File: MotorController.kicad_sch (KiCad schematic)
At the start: 103 parts, among them IC1 ft234xd, IC2 A3921KLPTR-T, IC3 A3921KLPTR-T, J1 Conn_01x04, J10 Conn_01x02, J2 USB_B_Micro, J3 Conn_01x02, J4 8P8C, J5 Conn_01x02, J6 Conn_01x04, J7 Conn_01x04, J8 Conn_01x02, J9 Conn_01x06, Q1 GSFQ6806, Q2 GSFQ6806, Q3 GSFQ6806, Q4 GSFQ6806, Q5 Q_PMOS_GDSD, SW1 SW_Push, SW2 SW_DPDT_x2, U1 LXES11D, U2 STM32F303K8Tx, U3 TJA11441AT, U4 TPSM13604HNDWR, U5 LMZ12002EXT, Y1 32M

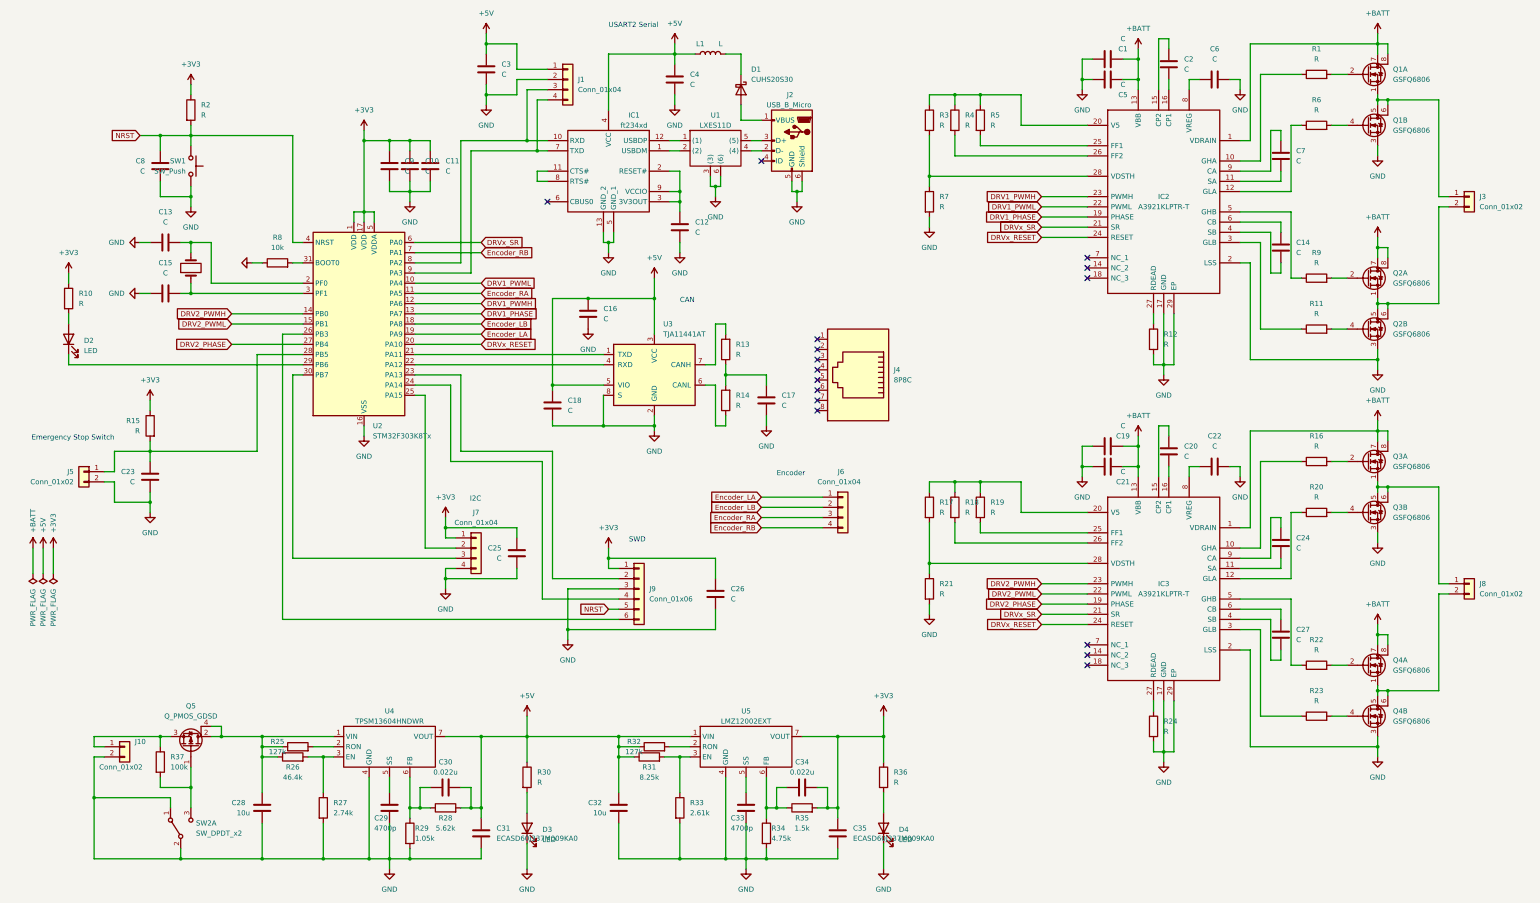
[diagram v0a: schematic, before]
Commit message: CAN 通信周りの端子の変更と電源スイッチの回路図を変更
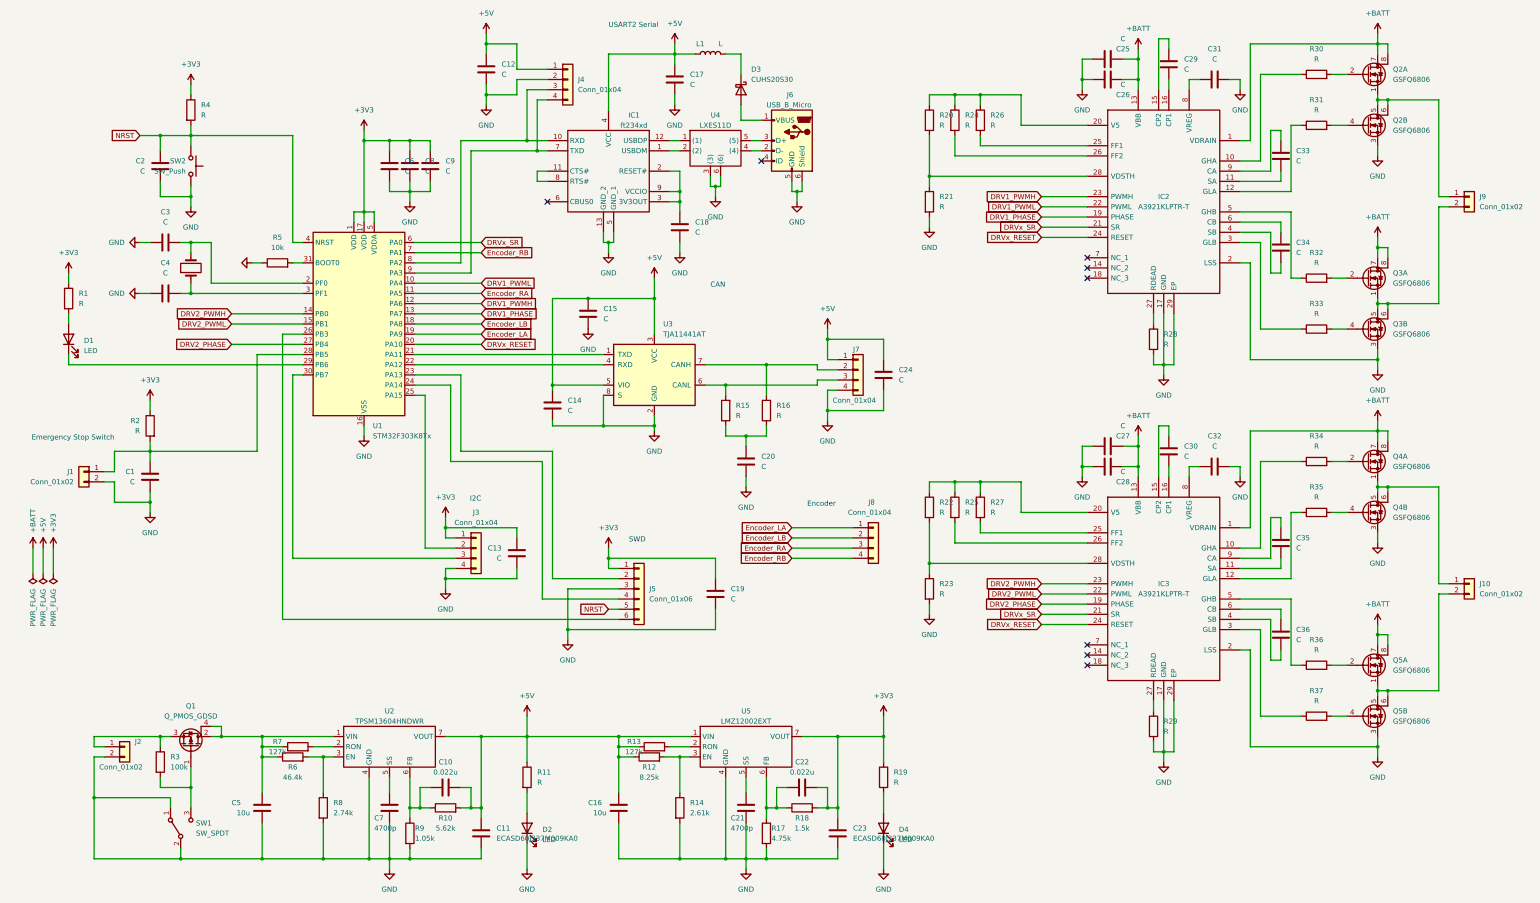
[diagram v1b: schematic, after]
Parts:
- removed C17: C, symbol Device:C
- removed J4: 8P8C, symbol Connector:8P8C
- removed SW2: SW_DPDT_x2, symbol Switch:SW_DPDT_x2
- added C20, C24: C, symbol Device:C
- added J7: Conn_01x04, symbol Connector_Generic:Conn_01x04
- added SW1: SW_SPDT, symbol Switch:SW_SPDT
- renumbered C23 to C1, C30 to C10, C31 to C11, C3 to C12, C25 to C13, C18 to C14, C16 to C15, C32 to C16, C4 to C17, C12 to C18, C26 to C19, C8 to C2, C33 to C21, C34 to C22, C35 to C23, C1 to C25, C5 to C26, C19 to C27, C21 to C28, C2 to C29, C13 to C3, C20 to C30, C6 to C31, C22 to C32, C7 to C33, C14 to C34, C24 to C35, C27 to C36, C15 to C4, C28 to C5, C9 to C6, C29 to C7, C10 to C8, C11 to C9, D2 to D1, D3 to D2, D1 to D3, J5 to J1, J8 to J10, J10 to J2, J7 to J3, J1 to J4, J9 to J5, J2 to J6, J6 to J8, J3 to J9, Q5 to Q1, Q1 to Q2, Q2 to Q3, Q3 to Q4, Q4 to Q5, R10 to R1, R28 to R10, R30 to R11, R31 to R12, R32 to R13, R33 to R14, R14 to R15, R13 to R16, R34 to R17, R35 to R18, R36 to R19, R15 to R2, R3 to R20, R7 to R21, R17 to R22, R21 to R23, R4 to R24, R18 to R25, R5 to R26, R19 to R27, R12 to R28, R24 to R29, R37 to R3, R1 to R30, R6 to R31, R9 to R32, R11 to R33, R16 to R34, R20 to R35, R22 to R36, R23 to R37, R2 to R4, R8 to R5, R26 to R6, R25 to R7, R27 to R8, R29 to R9, SW1 to SW2, U2 to U1, U4 to U2, U1 to U4
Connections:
- net +5V: now also C24.1, J7.1 (Pin_1)
- net GND: now also C20.2, C24.2, J7.4 (Pin_4), SW1.1 (A), SW1.2 (B)
- net at Q1.1 (G), R3.2: now also SW1.3 (C)
- net at R15.2: now also U3.6 (CANL), J7.3 (Pin_3); no longer R16.1
- net at R15.1: now also R16.1, C20.1; no longer U3.6 (CANL)
- net at R16.2, U3.7 (CANH): now also J7.2 (Pin_2)
- no-connect marks 16 -> 8
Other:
- moved on the sheet: J8, R15, R16

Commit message: 先輩に見せるためにいったんコミット。コネクタの回路図とか変えた
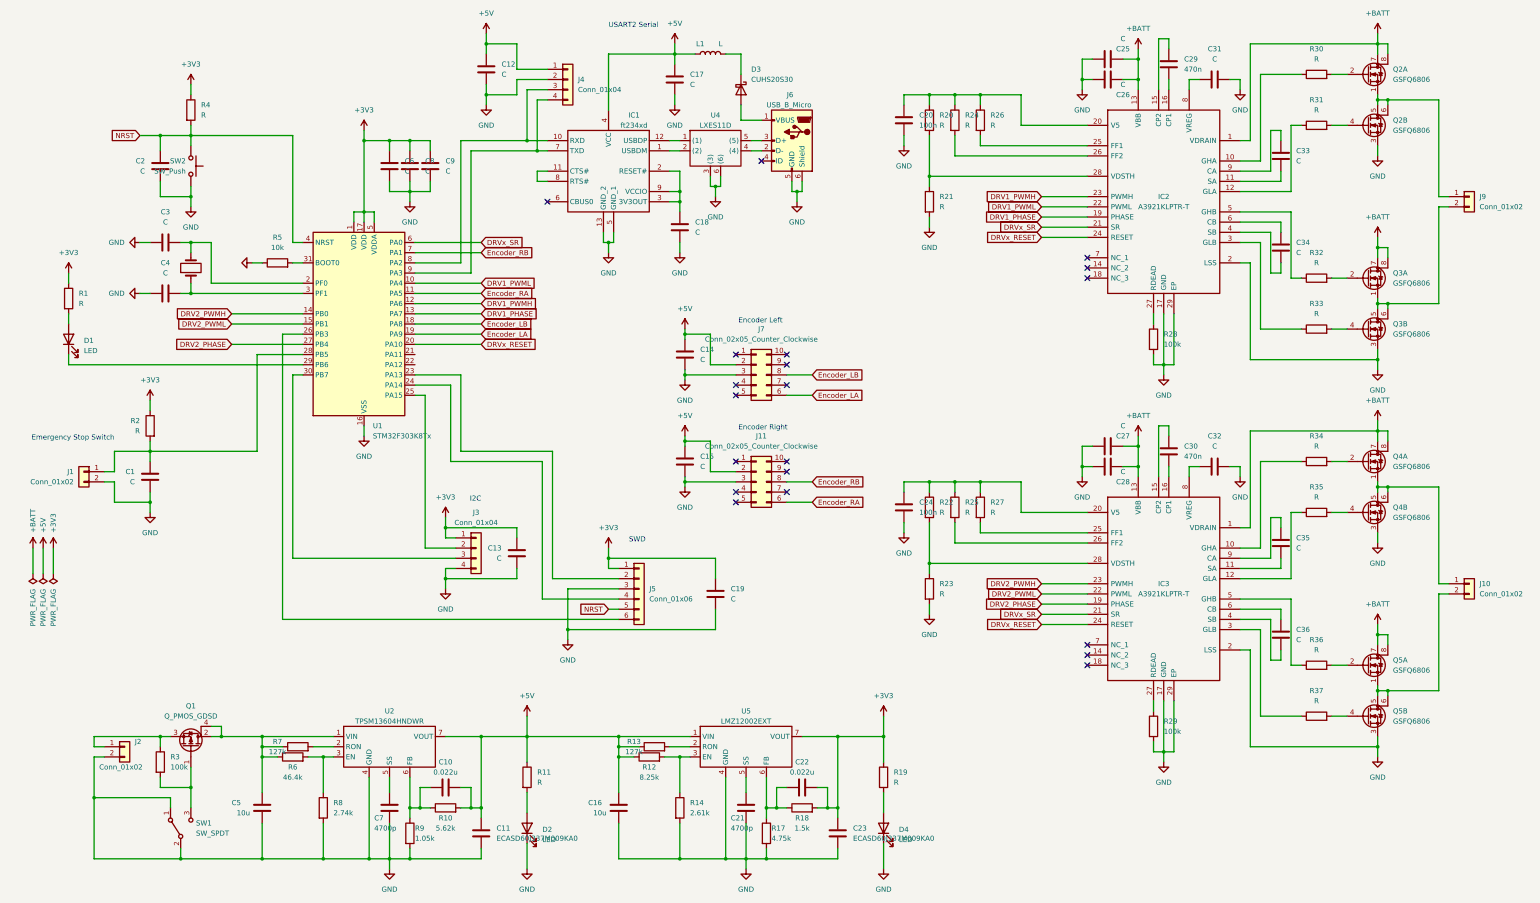
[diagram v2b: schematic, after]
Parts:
- removed J7, J8: Conn_01x04, symbol Connector_Generic:Conn_01x04
- removed R15, R16: R, symbol Device:R
- removed U3: TJA11441AT, Package_SO:SOIC-8_3.9x4.9mm_P1.27mm, symbol Interface_CAN_LIN:TJA1051T-3
- added J11, J7: Conn_02x05_Counter_Clockwise, symbol Connector_Generic:Conn_02x05_Counter_Clockwise
- C20, C24: value C -> 100n
- C29, C30: value C -> 470n
- R28, R29: value R -> 100k
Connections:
- net +5V: now also J11.2 (Pin_2), J7.2 (Pin_2); no longer C24.1
- net Encoder_LA: now also J7.6 (Pin_6)
- net Encoder_LB: now also J7.8 (Pin_8)
- net Encoder_RA: now also J11.6 (Pin_6)
- net Encoder_RB: now also J11.8 (Pin_8)
- net GND: now also J11.3 (Pin_3), J7.3 (Pin_3)
- net at IC3.20 (V5), R22.1, R25.1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: now also C24.1
- net at IC2.20 (V5), R20.1, R24.1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: now also C20.1
- no-connect marks 8 -> 20
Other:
- note added: "Encoder Left"
- note added: "Encoder Right"
- note removed: "CAN"
- note removed: "Encoder"

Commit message: A3921 の回路を訂正・USB 5V から DCDC 5V に入り込まないようにした・IC1 にパスコン追加
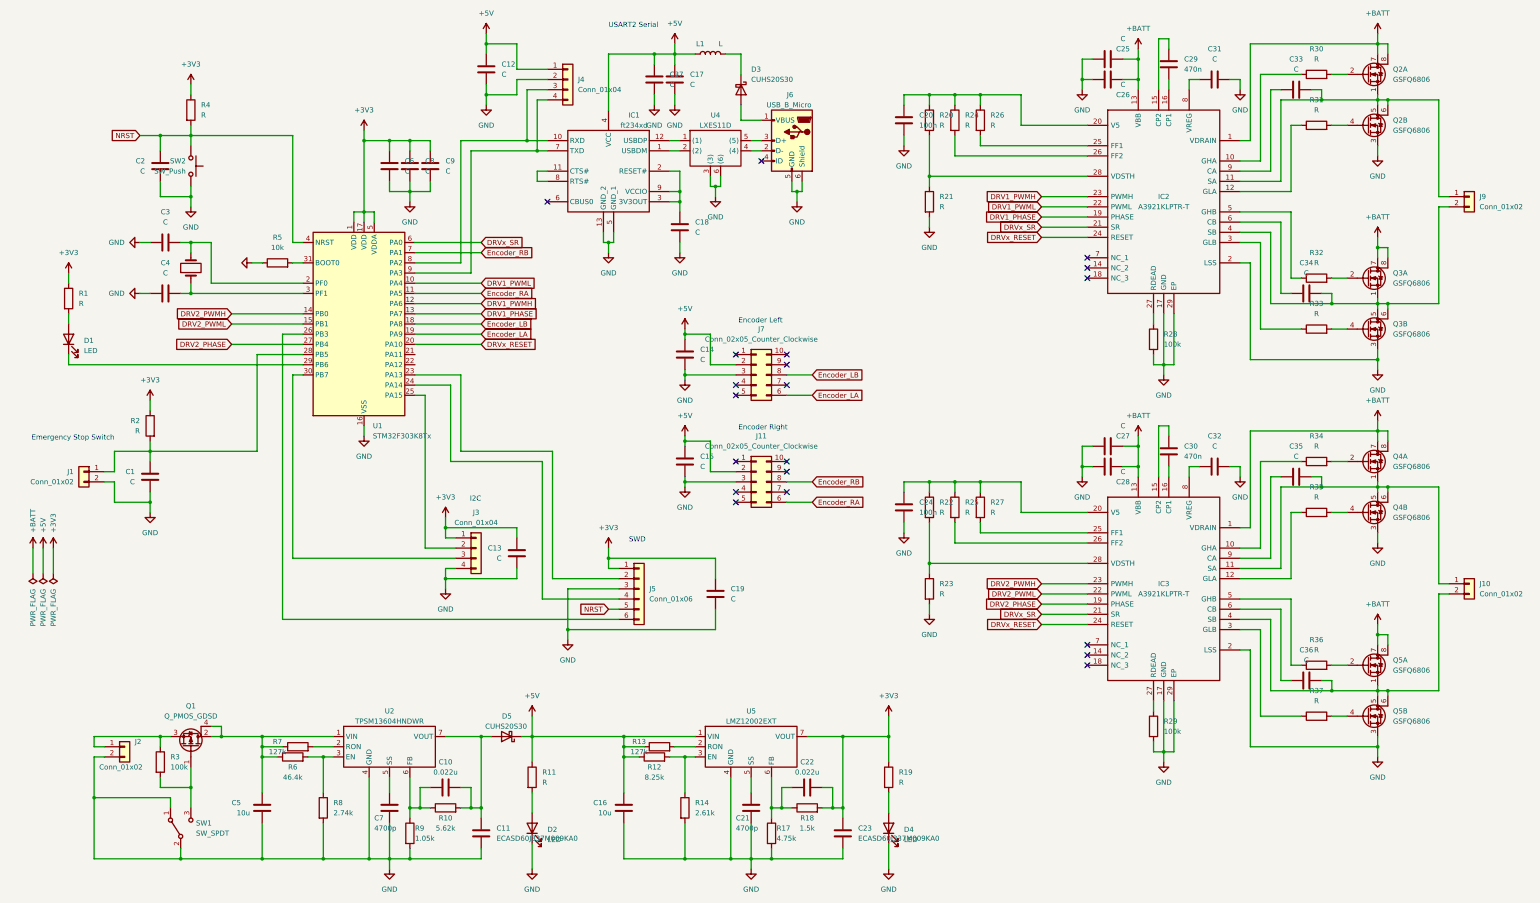
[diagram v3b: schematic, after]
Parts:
- added C37: C, symbol Device:C
- added D5: CUHS20S30, Diode_SMD:D_MELF, symbol Diode:1N5711UR
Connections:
- net +5V: now also C37.1, D5.1 (K); no longer C10.2, C11.1, R10.2, U2.7 (VOUT)
- net GND: now also C37.2
- net at J10.1 (Pin_1), Q4.1 (S), Q4.5 (D)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: now also C35.1, IC3.11 (SA)
- net at C34.1, IC2.4 (SB): now also J9.2 (Pin_2), Q3.1 (S), Q3.5 (D), Q3.6 (D)
- net at C36.1, IC3.4 (SB): now also J10.2 (Pin_2), Q5.1 (S), Q5.5 (D), Q5.6 (D)
- net at C33.1, IC2.11 (SA): now also J9.1 (Pin_1), Q2.1 (S), Q2.5 (D), Q2.6 (D)
- new net: C10.2, C11.1, D5.2 (A), R10.2, U2.7 (VOUT)
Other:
- moved on the sheet: C16, C21, C22, C23, C33, C34, C35, C36, D2, D4, R11, R12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

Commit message: hoge
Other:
- note added: "30 V Max"
- note added: "↓10.5 A Max"
- note added: "↓20 A Max"
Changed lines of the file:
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@@
     (stroke (width 0) (type default))
   )
+  (wire (pts (xy 172.72 24.13) (xy 172.72 26.67))
+    (stroke (width 0) (type default))
+  )
   (wire (pts (xy 165.1 227.33) (xy 180.34 227.33))
     (stroke (width 0) (type default))
@@
     (stroke (width 0) (type default))
   )
-  (wire (pts (xy 177.8 24.13) (xy 177.8 26.67))
-    (stroke (width 0) (type default))
-  )
   (wire (pts (xy 179.07 73.66) (xy 179.07 76.2))
     (stroke (width 0) (type default))
@@
     (stroke (width 0) (type default))
   )
-  (text "USART2 Serial" (at 161.29 20.32 0)
+  (text "USART2 Serial" (at 156.21 20.32 0)
+    (effects (font (size 1.27 1.27)) (justify left bottom))
+  )
+  (text "↓20 A Max" (at 355.6 36.83 0)
     (effects (font (size 1.27 1.27)) (justify left bottom))
   )
@@
     (effects (font (size 1.27 1.27)) (justify right bottom))
   )
+  (text "↓10.5 A Max" (at 354.33 21.59 0)
+    (effects (font (size 1.27 1.27)) (justify left bottom))
+  )
   (text "I2C" (at 129.54 138.43 0)
     (effects (font (size 1.27 1.27)) (justify right bottom))
@@
     (effects (font (size 1.27 1.27)) (justify left bottom))
   )
+  (text "30 V Max" (at 356.87 17.78 0)
+    (effects (font (size 1.27 1.27)) (justify left bottom))
+  )
   (text "Encoder Left" (at 193.675 93.98 0)
     (effects (font (size 1.27 1.27)) (justify left bottom))
@@
     )
   )
-  (symbol (lib_id "power:+5V") (at 177.8 24.13 0) (unit 1)
+  (symbol (lib_id "power:+5V") (at 172.72 24.13 0) (unit 1)
     (in_bom yes) (on_board yes) (dnp no) (fields_autoplaced)
-    (property "Reference" "#PWR028" (at 177.8 27.94 0)
+    (property "Reference" "#PWR028" (at 172.72 27.94 0)
       (effects (font (size 1.27 1.27)) hide)
     )
-    (property "Value" "+5V" (at 177.8 19.05 0)
+    (property "Value" "+5V" (at 172.72 19.05 0)
       (effects (font (size 1.27 1.27)))
     )
-    (property "Footprint" "" (at 177.8 24.13 0)
+    (property "Footprint" "" (at 172.72 24.13 0)
       (effects (font (size 1.27 1.27)) hide)
     )
-    (property "Datasheet" "" (at 177.8 24.13 0)
+    (property "Datasheet" "" (at 172.72 24.13 0)
       (effects (font (size 1.27 1.27)) hide)
     )

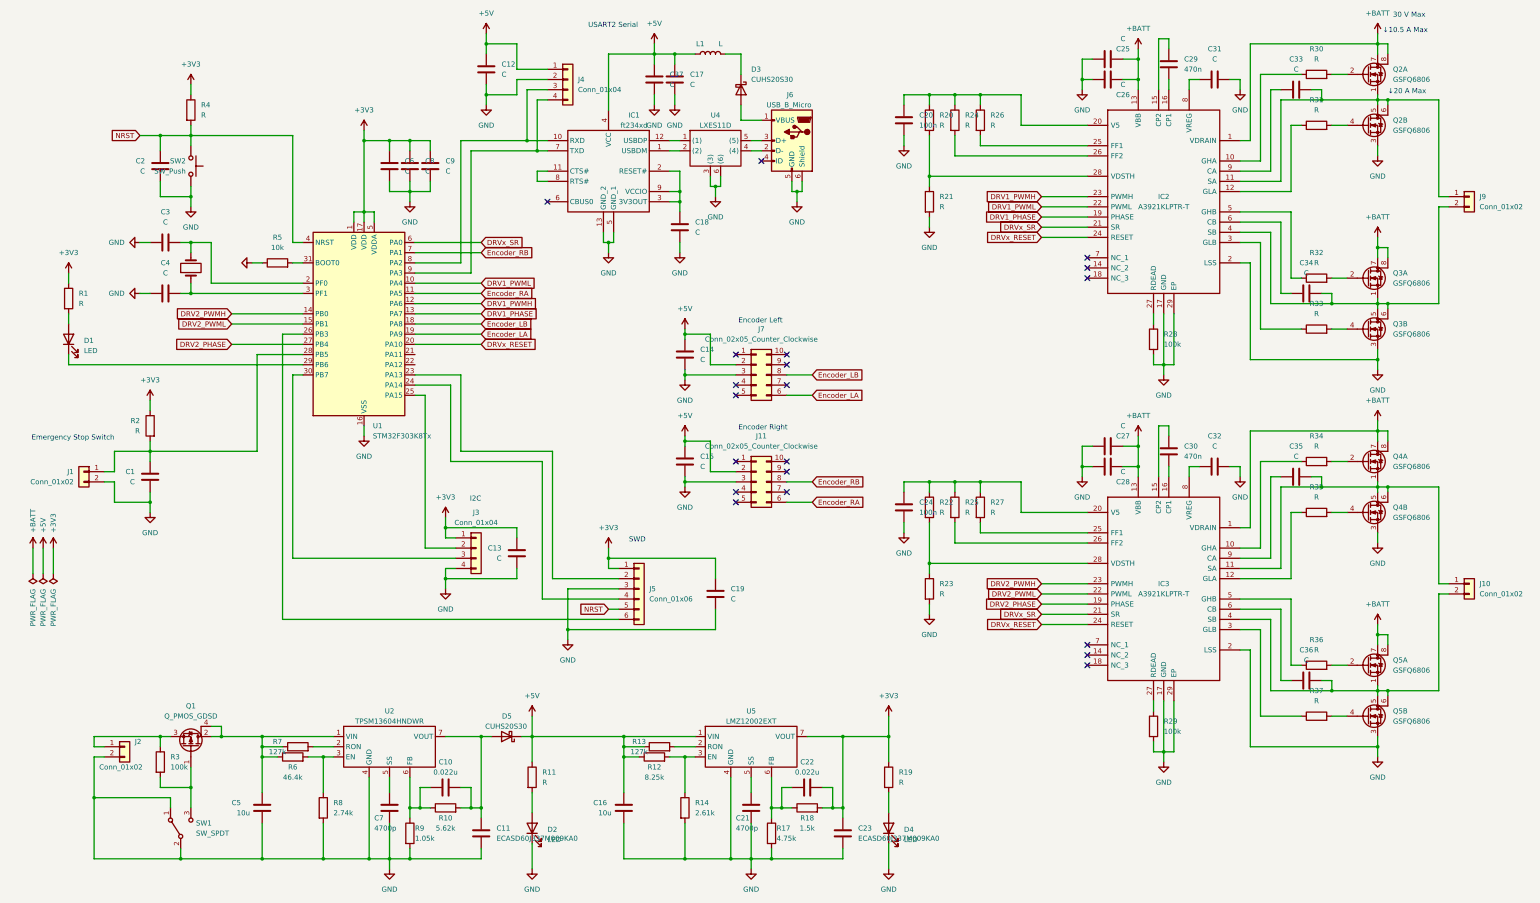
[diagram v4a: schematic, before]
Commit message: 緊急停止スイッチをマイコンではなくゲートドライバにつなげた
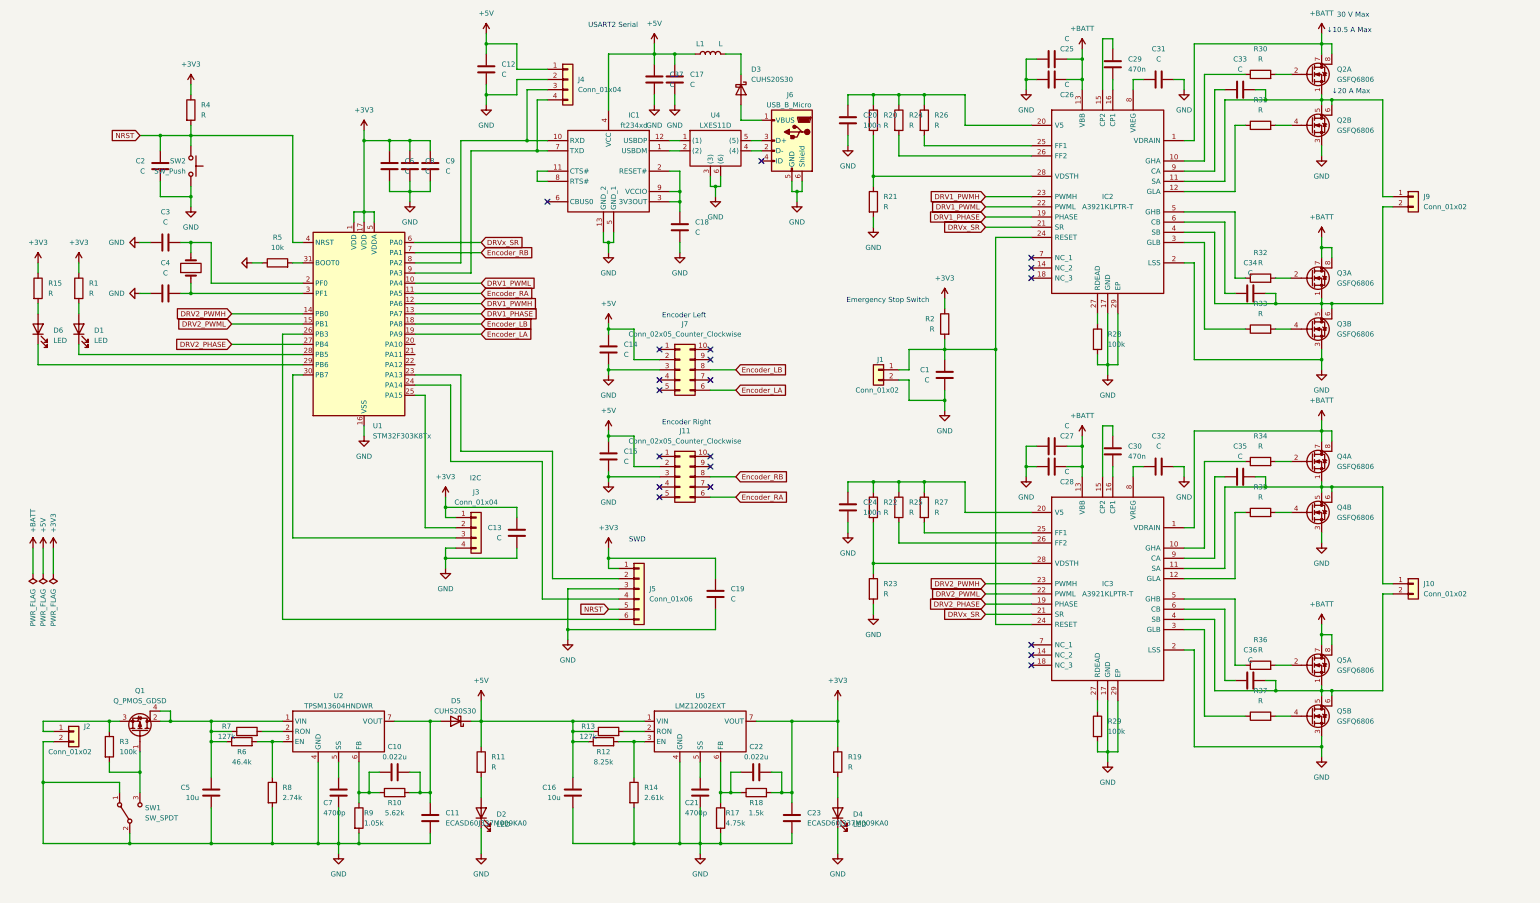
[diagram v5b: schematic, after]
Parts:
- added D6: LED, symbol Device:LED
- added R15: R, symbol Device:R
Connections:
- net +3V3: now also R15.1
- net at C1.1, J1.1 (Pin_1), R2.2: now also IC2.24 (RESET), IC3.24 (RESET); no longer U1.28 (PB5)
- net at D1.1 (K): now also U1.28 (PB5); no longer U1.29 (PB6)
- removed net DRVx_RESET: IC2.24 (RESET), IC3.24 (RESET), U1.20 (PA10)
- new net: D6.1 (K), U1.29 (PB6)
- new net: D6.2 (A), R15.2
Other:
- moved on the sheet: C10, C11, C13, C14, C15, C16, C20, C21, C22, C23, C24, C25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
